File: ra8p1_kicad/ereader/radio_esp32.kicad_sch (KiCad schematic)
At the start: 9 parts, among them U3 ESP32-C6-WROOM-1-N8, U4 TPS22917DBVT, U5 TXU0304PWR

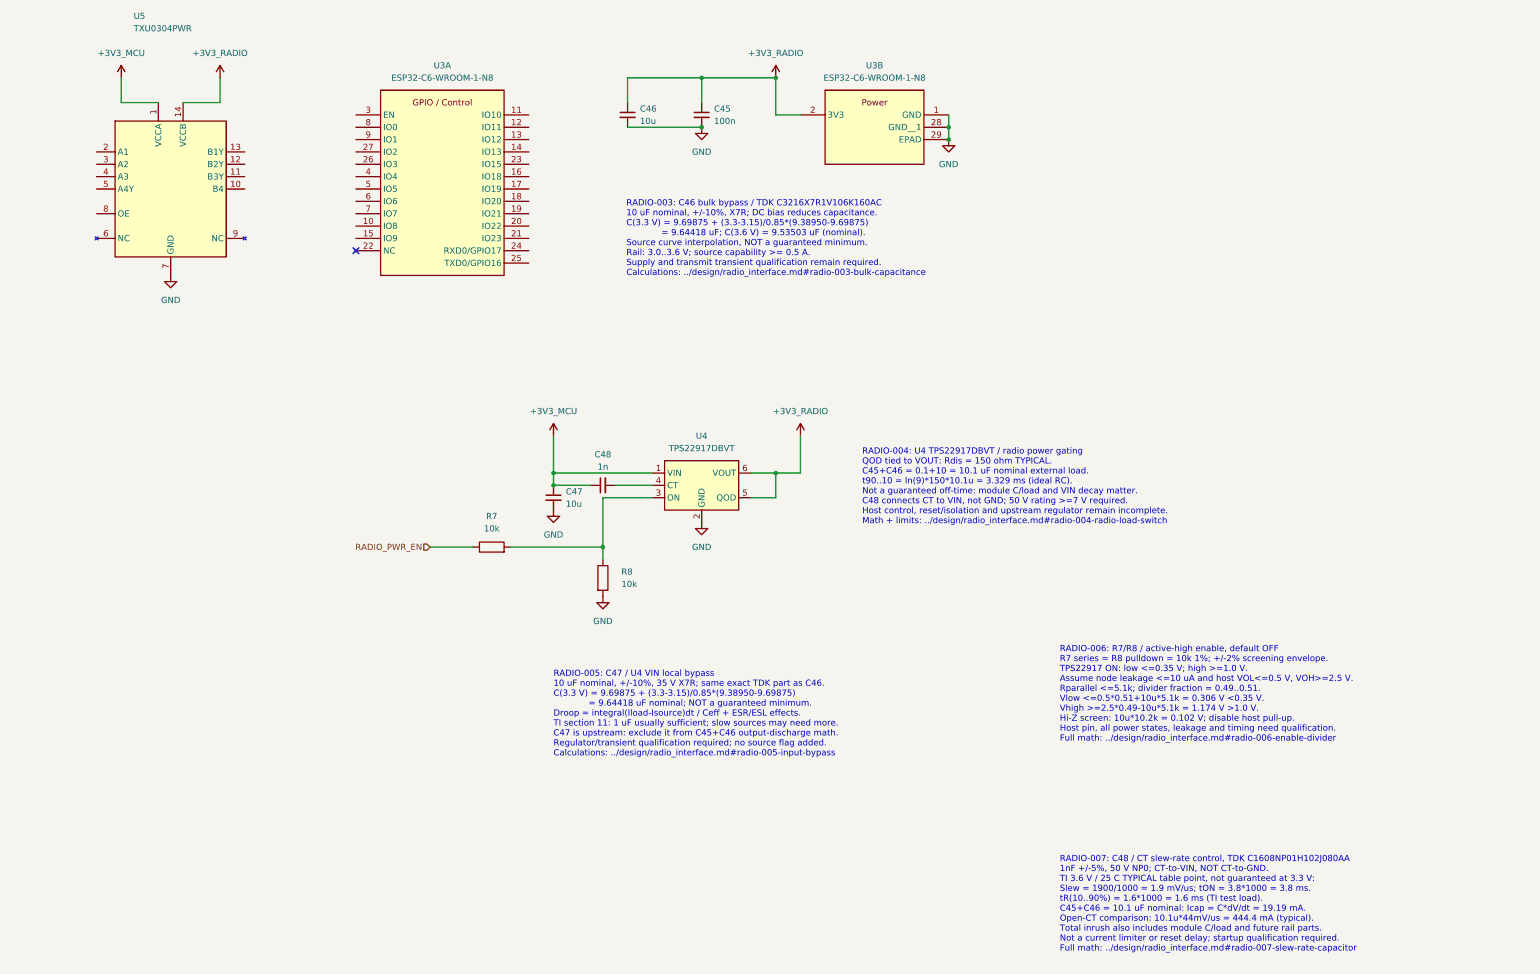
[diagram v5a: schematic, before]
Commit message: Add translator bypass and wire radio clock and COPI
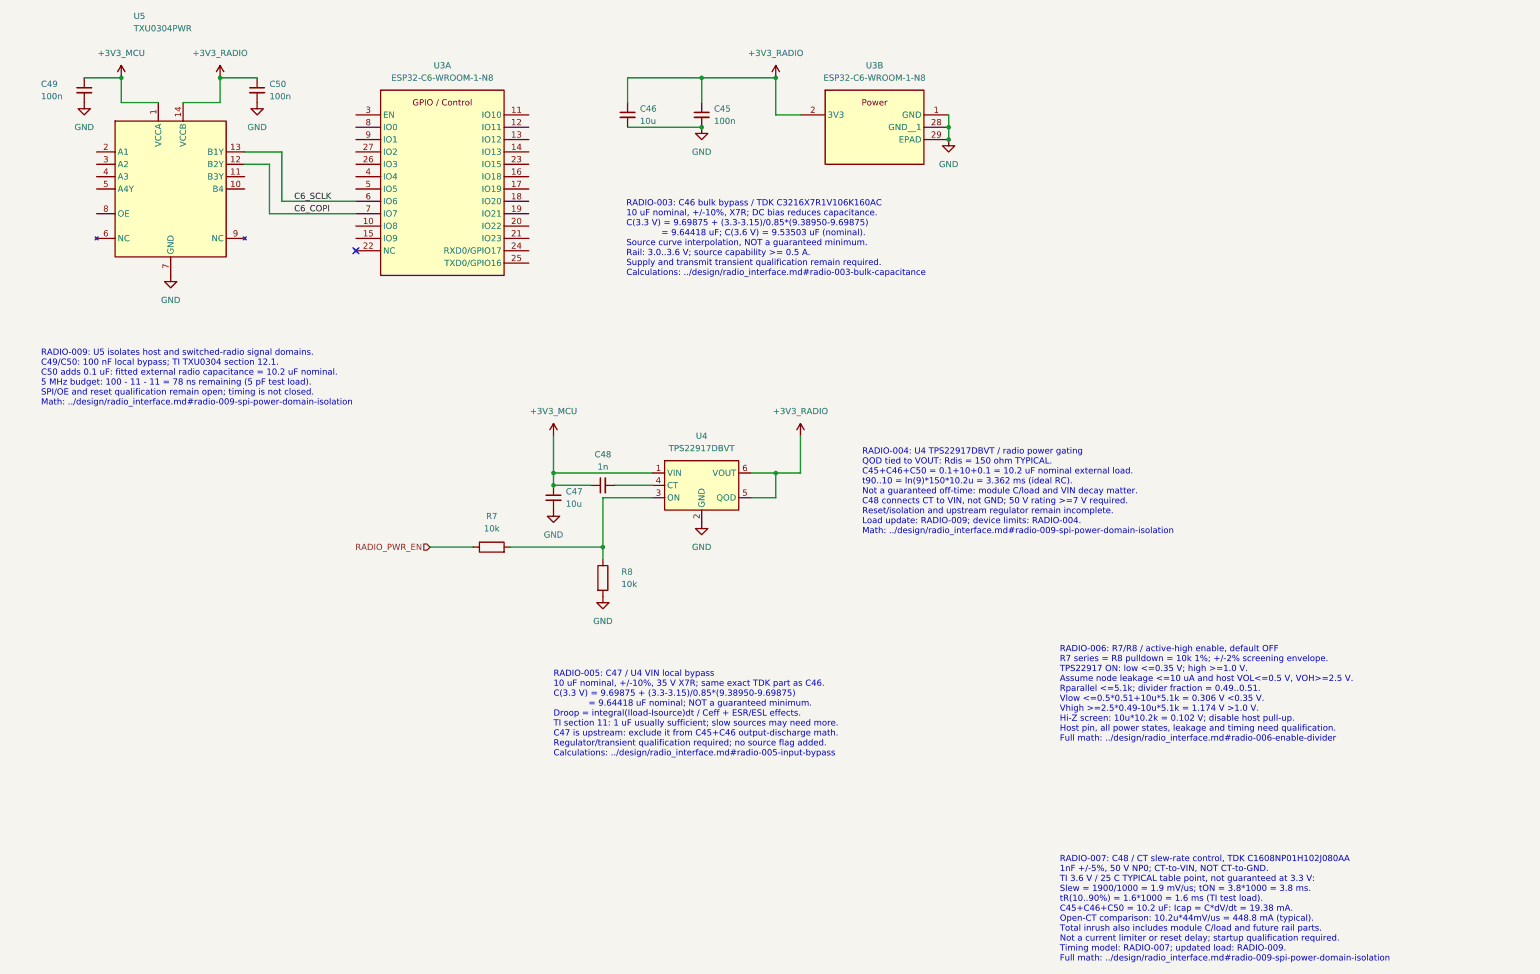
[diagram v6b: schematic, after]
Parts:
- added C49, C50: 100n, symbol Device:C_Small
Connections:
- net +3V3_MCU: now also C49.1
- net +3V3_RADIO: now also C50.1
- net GND: now also C49.2, C50.2
- net C6_SCLK: now reaches U3.6 (IO6)
- net C6_SCLK: now also U5.13 (B1Y)
- net C6_COPI: now reaches U3.7 (IO7)
- net C6_COPI: now also U5.12 (B2Y)
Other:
- note added: "RADIO-004: U4 TPS22917DBVT / radio power gating QOD tied to VOUT: Rdis = 150 ohm TYPICAL. C45+C46+C50 = 0.1+10+0.1 = 10.2 uF nominal external load. t90..10 = ln(9)*150*10.2u = 3.362 ms (ideal RC). Not a guaranteed off-time: module C/load and VIN decay matter. C48 connects CT to VIN, not GND; 50 V rating >=7 V required. Reset/isolation and upstream regulator remain incomplete. Load update: RADIO-0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"
- note added: "RADIO-007: C48 / CT slew-rate control, TDK C1608NP01H102J080AA 1nF +/-5%, 50 V NP0; CT-to-VIN, NOT CT-to-GND. TI 3.6 V / 25 C TYPICAL table point, not guaranteed at 3.3 V: Slew = 1900/1000 = 1.9 mV/us; tON = 3.8*1000 = 3.8 ms. tR(10..90%) = 1.6*1000 = 1.6 ms (TI test load). C45+C46+C50 = 10.2 uF: Icap = C*dV/dt = 19.38 mA. Open-CT comparison: 10.2u*44mV/us = 448.8 mA (typical). Total inrush also 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"
- note added: "RADIO-009: U5 isolates host and switched-radio signal domains. C49/C50: 100 nF local bypass; TI TXU0304 section 12.1. C50 adds 0.1 uF: fitted external radio capacitance = 10.2 uF nominal. 5 MHz budget: 100 - 11 - 11 = 78 ns remaining (5 pF test load). SPI/OE and reset qualification remain open; timing is not closed. Math: ../design/radio_interface.md#radio-009-spi-power-domain-isolation"
- note removed: "RADIO-004: U4 TPS22917DBVT / radio power gating QOD tied to VOUT: Rdis = 150 ohm TYPICAL. C45+C46 = 0.1+10 = 10.1 uF nominal external load. t90..10 = ln(9)*150*10.1u = 3.329 ms (ideal RC). Not a guaranteed off-time: module C/load and VIN decay matter. C48 connects CT to VIN, not GND; 50 V rating >=7 V required. Host control, reset/isolation and upstream regulator remain incomplete. Math + limits: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"
- note removed: "RADIO-007: C48 / CT slew-rate control, TDK C1608NP01H102J080AA 1nF +/-5%, 50 V NP0; CT-to-VIN, NOT CT-to-GND. TI 3.6 V / 25 C TYPICAL table point, not guaranteed at 3.3 V: Slew = 1900/1000 = 1.9 mV/us; tON = 3.8*1000 = 3.8 ms. tR(10..90%) = 1.6*1000 = 1.6 ms (TI test load). C45+C46 = 10.1 uF nominal: Icap = C*dV/dt = 19.19 mA. Open-CT comparison: 10.1u*44mV/us = 444.4 mA (typical). Total inrush a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"

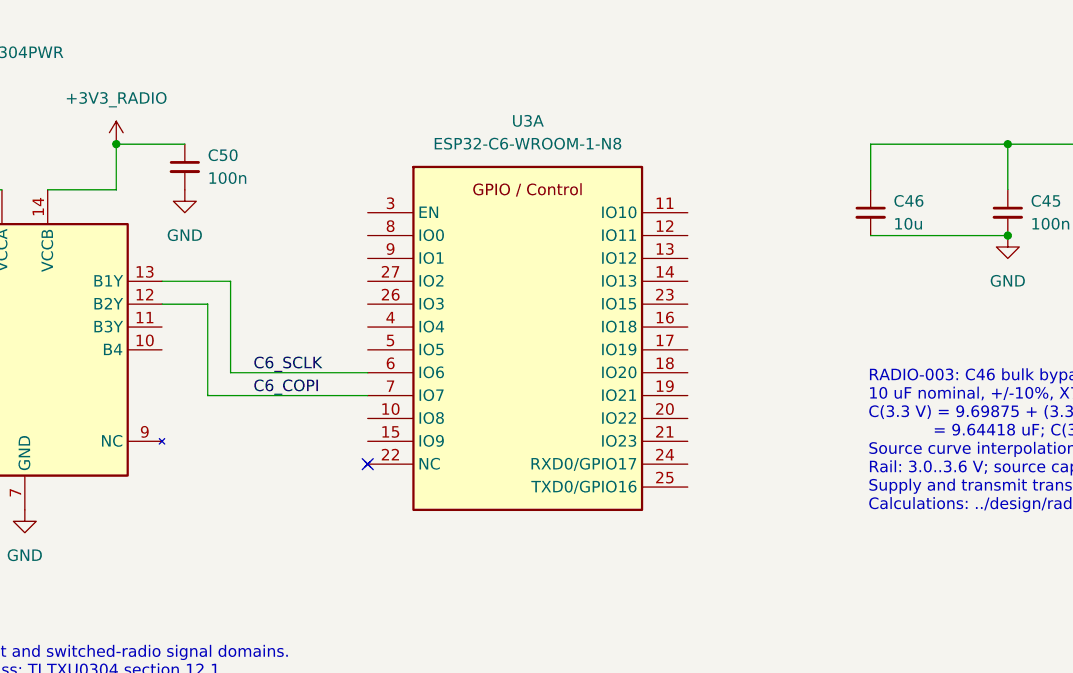
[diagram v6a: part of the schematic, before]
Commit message: Connect C6-side SPI signals with readable labeled routing
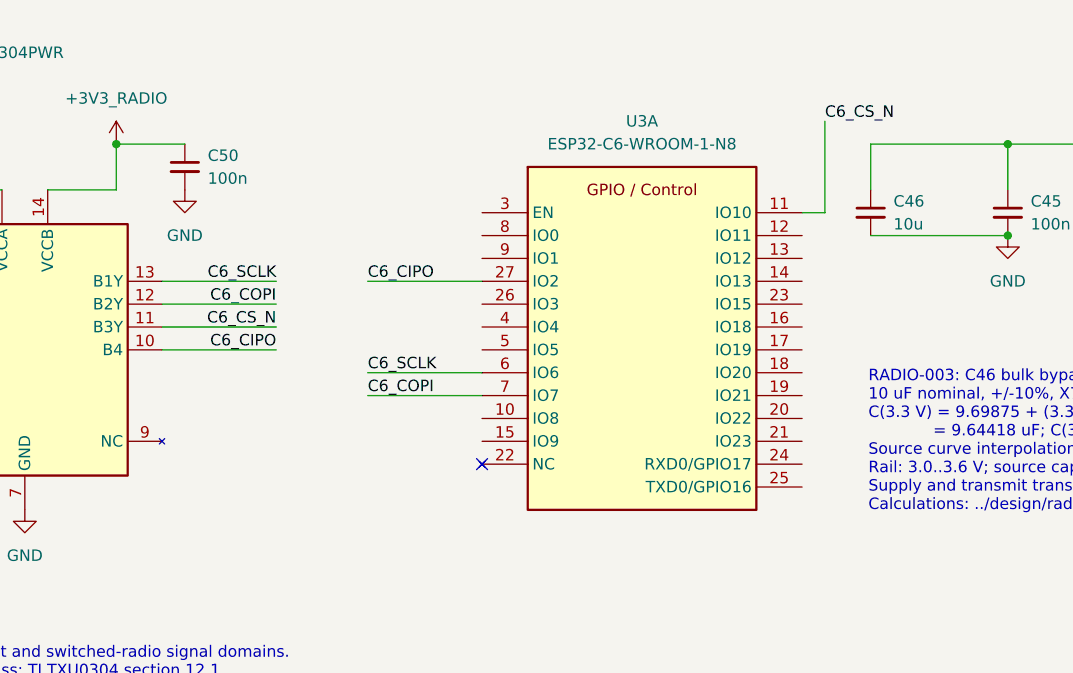
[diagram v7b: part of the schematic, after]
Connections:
- net C6_CS_N: now reaches U3.11 (IO10)
- net C6_CS_N: now also U5.11 (B3Y)
- net C6_CIPO: now reaches U3.27 (IO2)
- net C6_CIPO: now also U5.10 (B4)
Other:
- moved on the sheet: U3A
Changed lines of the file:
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@@
 	)
 	(no_connect
-		(at 83.82 104.14)
+		(at 96.52 104.14)
 	)
 	(wire
@@
 	(wire
 		(pts
-			(xy 68.58 83.82) (xy 68.58 93.98)
-		)
-		(stroke
-			(width 0)
-			(type default)
-		)
-	)
-	(wire
-		(pts
-			(xy 66.04 96.52) (xy 83.82 96.52)
-		)
-		(stroke
-			(width 0)
-			(type default)
-		)
-	)
-	(wire
-		(pts
 			(xy 165.1 154.94) (xy 170.18 154.94)
 		)
@@
 	(wire
 		(pts
+			(xy 83.82 83.82) (xy 96.52 83.82)
+		)
+		(stroke
+			(width 0)
+			(type default)
+		)
+	)
+	(wire
+		(pts
 			(xy 139.7 68.58) (xy 154.94 68.58)
 		)
@@
 	(wire
 		(pts
-			(xy 60.96 83.82) (xy 68.58 83.82)
+			(xy 83.82 96.52) (xy 96.52 96.52)
 		)
 		(stroke
@@
 	(wire
 		(pts
+			(xy 60.96 88.9) (xy 73.66 88.9)
+		)
+		(stroke
+			(width 0)
+			(type default)
+		)
+	)
+	(wire
+		(pts
 			(xy 170.18 68.58) (xy 170.18 76.2)
 		)
@@
 	(wire
 		(pts
-			(xy 60.96 86.36) (xy 66.04 86.36)
-		)
-		(stroke
-			(width 0)
-			(type default)
-		)
-	)
-	(wire
-		(pts
 			(xy 137.16 152.4) (xy 144.78 152.4)
 		)
@@
 	(wire
 		(pts
+			(xy 60.96 86.36) (xy 73.66 86.36)
+		)
+		(stroke
+			(width 0)
+			(type default)
+		)
+	)
+	(wire
+		(pts
 			(xy 170.18 149.86) (xy 175.26 149.86)
 		)
@@
 	(wire
 		(pts
+			(xy 134.62 66.04) (xy 134.62 76.2)
+		)
+		(stroke
+			(width 0)
+			(type default)
+		)
+	)
+	(wire
+		(pts
+			(xy 60.96 91.44) (xy 73.66 91.44)
+		)
+		(stroke
+			(width 0)
+			(type default)
+		)
+	)
+	(wire
+		(pts
+			(xy 132.08 76.2) (xy 134.62 76.2)
+		)
+		(stroke
+			(width 0)
+			(type default)
+		)
+	)
+	(wire
+		(pts
 			(xy 154.94 73.66) (xy 154.94 68.58)
 		)
@@
 	(wire
 		(pts
-			(xy 66.04 86.36) (xy 66.04 96.52)
-		)
-		(stroke
-			(width 0)
-			(type default)
-		)
-	)
-	(wire
-		(pts
 			(xy 99.06 165.1) (xy 107.95 165.1)
 		)
@@
 	(wire
 		(pts
-			(xy 68.58 93.98) (xy 83.82 93.98)
+			(xy 83.82 93.98) (xy 96.52 93.98)
+		)
+		(stroke
+			(width 0)
+			(type default)
+		)
+	)
+	(wire
+		(pts
+			(xy 60.96 83.82) (xy 73.66 83.82)
 		)
 		(stroke
@@
 	)
 	(label "C6_SCLK"
-		(at 71.12 93.98 0)
+		(at 83.82 93.98 0)
 		(effects
 			(font
@@
 		)
 	)
-	(label "C6_COPI"
-		(at 71.12 96.52 0)
+	(label "C6_CIPO"
+		(at 83.82 83.82 0)
 		(effects
 			(font
@@
 			)
 			(justify left bottom)
+		)
+	)
+	(label "C6_CS_N"
+		(at 73.66 88.9 180)
+		(effects
+			(font
+				(size 1.27 1.27)
+			)
+			(justify right bottom)
+		)
+	)
+	(label "C6_COPI"
+		(at 83.82 96.52 0)
+		(effects
+			(font
+				(size 1.27 1.27)
+			)
+			(justify left bottom)
+		)
+	)
+	(label "C6_CIPO"
+		(at 73.66 91.44 180)
+		(effects
+			(font
+				(size 1.27 1.27)
+			)
+			(justify right bottom)
+		)
+	)
+	(label "C6_COPI"
+		(at 73.66 86.36 180)
+		(effects
+			(font
+				(size 1.27 1.27)
+			)
+			(justify right bottom)
+		)
+	)
+	(label "C6_CS_N"
+		(at 134.62 66.04 0)
+		(effects
+			(font
+				(size 1.27 1.27)
+			)
+			(justify left bottom)
+		)
+	)
+	(label "C6_SCLK"
+		(at 73.66 83.82 180)
+		(effects
+			(font
+				(size 1.27 1.27)
+			)
+			(justify right bottom)
 		)
 	)
@@
 	(symbol
 		(lib_id "Wireless:ESP32-C6-WROOM-1-N8")
-		(at 101.6 76.2 0)
+		(at 114.3 76.2 0)
 		(unit 1)
 		(body_style 1)
@@
 		(fields_autoplaced yes)
 		(property "Reference" "U3"
-			(at 101.6 66.04 0)
+			(at 114.3 66.04 0)
 			(show_name no)
 			(do_not_autoplace no)
@@
 		)
 		(property "Value" "ESP32-C6-WROOM-1-N8"
-			(at 101.6 68.58 0)
+			(at 114.3 68.58 0)
 			(show_name no)
 			(do_not_autoplace no)
@@
 		)
 		(property "Footprint" "Wireless:XCVR_ESP32-C6-WROOM-1-N8"
-			(at 101.6 76.2 0)
+			(at 114.3 76.2 0)
 			(hide yes)
 			(show_name no)
@@
 		)
 		(property "Datasheet" "https://www.espressif.com/sites/default/files/documentation/esp32-c6-wroom-1_wroom-1u_datasheet_en.pdf"
-			(at 101.6 76.2 0)
+			(at 114.3 76.2 0)
 			(hide yes)
 			(show_name no)
@@
 		)
 		(property "Description" "Wi-Fi 6 + BLE 5.3 + 802.15.4 RISC-V SoC module, 8MB flash"
-			(at 101.6 76.2 0)
+			(at 114.3 76.2 0)
 			(hide yes)
 			(show_name no)
@@
 		)
 		(property "PARTREV" "1.0"
-			(at 101.6 76.2 0)
+			(at 114.3 76.2 0)
 			(hide yes)
 			(show_name no)
@@
 		)
 		(property "STANDARD" "Manufacturer Recommendations"
-			(at 101.6 76.2 0)
+			(at 114.3 76.2 0)
 			(hide yes)
 			(show_name no)
@@
 		)
 		(property "MAXIMUM_PACKAGE_HEIGHT" "3.25mm"
-			(at 101.6 76.2 0)
+			(at 114.3 76.2 0)
 			(hide yes)
 			(show_name no)
@@
 		)
 		(property "MANUFACTURER" "Espressif Systems"
-			(at 101.6 76.2 0)
+			(at 114.3 76.2 0)
 			(hide yes)
 			(show_name no)
@@
 		)
 		(property "Manufacturer_Name" "Espressif Systems"
-			(at 101.6 76.2 0)
+			(at 114.3 76.2 0)
 			(hide yes)
 			(show_name no)
@@
 		)
 		(property "Manufacturer_Part_Number" "ESP32-C6-WROOM-1-N8"
-			(at 101.6 76.2 0)
+			(at 114.3 76.2 0)
 			(hide yes)
 			(show_name no)
@@
 		)
 		(property "DigiKey_Part_Number" "1965-ESP32-C6-WROOM-1-N8CT-ND"
-			(at 101.6 76.2 0)
+			(at 114.3 76.2 0)
 			(hide yes)
 			(show_name no)
@@
 		)
 		(property "DigiKey_URL" "https://www.digikey.com/en/products/detail/espressif-systems/ESP32-C6-WROOM-1-N8/17728866"
-			(at 101.6 76.2 0)
+			(at 114.3 76.2 0)
 			(hide yes)
 			(show_name no)
@@
 		)
 		(property "Sourcing_Snapshot" "2026-09-05 DigiKey: Active; 1435 in stock; USD qty1 5.55, qty10 4.80, qty100 4.1844. Tariff may apply; recheck before ordering."
-			(at 101.6 76.2 0)
+			(at 114.3 76.2 0)
 			(hide yes)
 			(show_name no)
@@
 		)
 		(property "Procurement_Status" "Sourced candidate; electrical integration and footprint qualification pending"
-			(at 101.6 76.2 0)
-			(hide yes)
-			(show_name no)
+			(at 114.3 76.2 0)
+			(hide yes)
+			(show_name no)

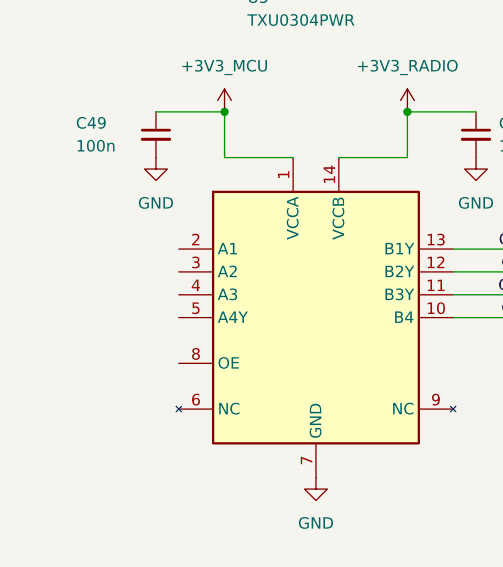
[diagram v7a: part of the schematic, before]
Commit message: Connect RA8P1 host SPI through the radio hierarchy
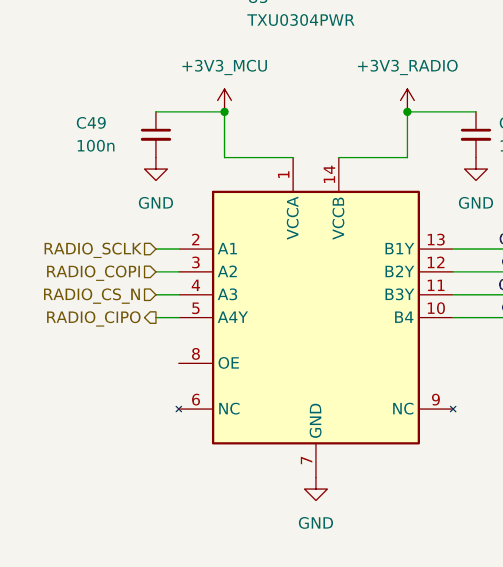
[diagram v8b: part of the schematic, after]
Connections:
- net RADIO_SCLK: now reaches U5.2 (A1)
- net RADIO_COPI: now reaches U5.3 (A2)
- net RADIO_CS_N: now reaches U5.4 (A3)
- net RADIO_CIPO: now reaches U5.5 (A4Y)
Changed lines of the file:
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@@
+	(wire
+		(pts
+			(xy 27.94 91.44) (xy 30.48 91.44)
+		)
+		(stroke
+			(width 0)
+			(type default)
+		)
+	)
 	(wire
 		(pts
@@
 	(wire
 		(pts
+			(xy 27.94 86.36) (xy 30.48 86.36)
+		)
+		(stroke
+			(width 0)
+			(type default)
+		)
+	)
+	(wire
+		(pts
 			(xy 124.46 149.86) (xy 144.78 149.86)
 		)
@@
 	(wire
 		(pts
+			(xy 27.94 88.9) (xy 30.48 88.9)
+		)
+		(stroke
+			(width 0)
+			(type default)
+		)
+	)
+	(wire
+		(pts
 			(xy 35.56 68.58) (xy 35.56 73.66)
 		)
@@
 		(pts
 			(xy 170.18 149.86) (xy 170.18 154.94)
+		)
+		(stroke
+			(width 0)
+			(type default)
+		)
+	)
+	(wire
+		(pts
+			(xy 27.94 83.82) (xy 30.48 83.82)
 		)
 		(stroke
@@
 		(effects
 			(font
+				(size 1.27 1.27)
+			)
+			(justify right)
+		)
+	)
+	(hierarchical_label "RADIO_SCLK"
+		(shape input)
+		(at 27.94 83.82 180)
+		(effects
+			(font
+				(size 1.27 1.27)
+			)
+			(justify right)
+		)
+	)
+	(hierarchical_label "RADIO_COPI"
+		(shape input)
+		(at 27.94 86.36 180)
+		(effects
+			(font
+				(size 1.27 1.27)
+			)
+			(justify right)
+		)
+	)
+	(hierarchical_label "RADIO_CIPO"
+		(shape output)
+		(at 27.94 91.44 180)
+		(effects
+			(font
+				(size 1.27 1.27)
+			)
+			(justify right)
+		)
+	)
+	(hierarchical_label "RADIO_CS_N"
+		(shape input)
+		(at 27.94 88.9 180)
+		(effects
+			(font
